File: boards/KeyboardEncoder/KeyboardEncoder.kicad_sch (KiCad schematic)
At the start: 30 parts, among them J1 ISP, J2 Encoder, J3 MIDI Out, J4 SelectRX, J5 MIDI In, J7 BoardCon, J8 PistonEncoder, U1 ATmega48-20P, U2 6N137, U3 74LS14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

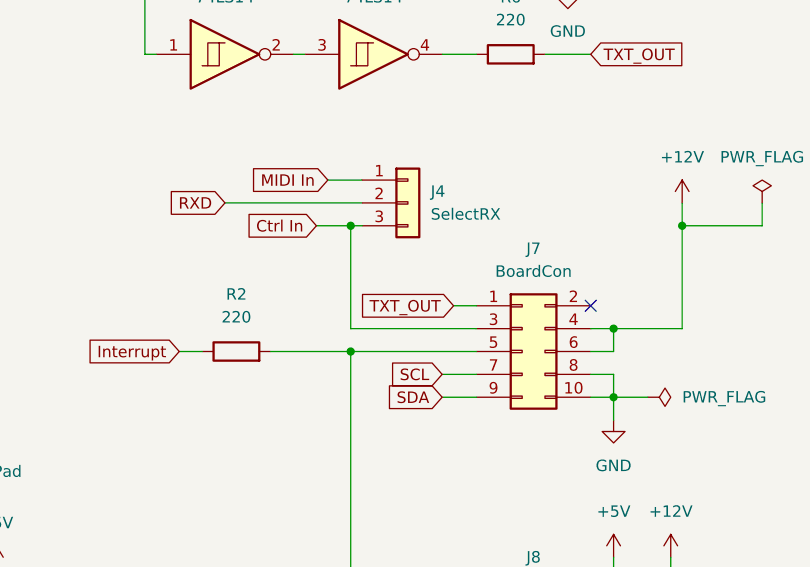
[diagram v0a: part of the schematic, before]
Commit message: Finished IO-Board PCB, switched RX/TX of board connectors for better routing
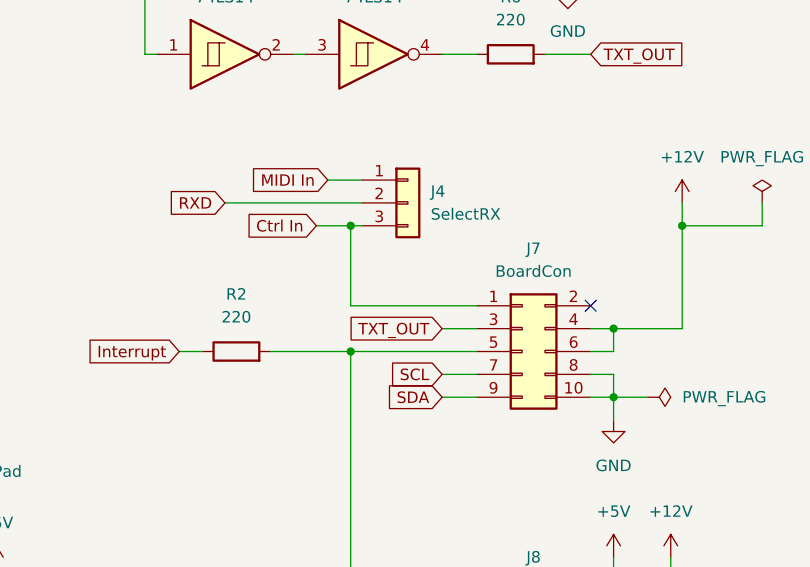
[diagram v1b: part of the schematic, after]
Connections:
- net Ctrl In: now also J7.1 (Pin_1); no longer J7.3 (Pin_3)
- net TXT_OUT: now also J7.3 (Pin_3); no longer J7.1 (Pin_1)

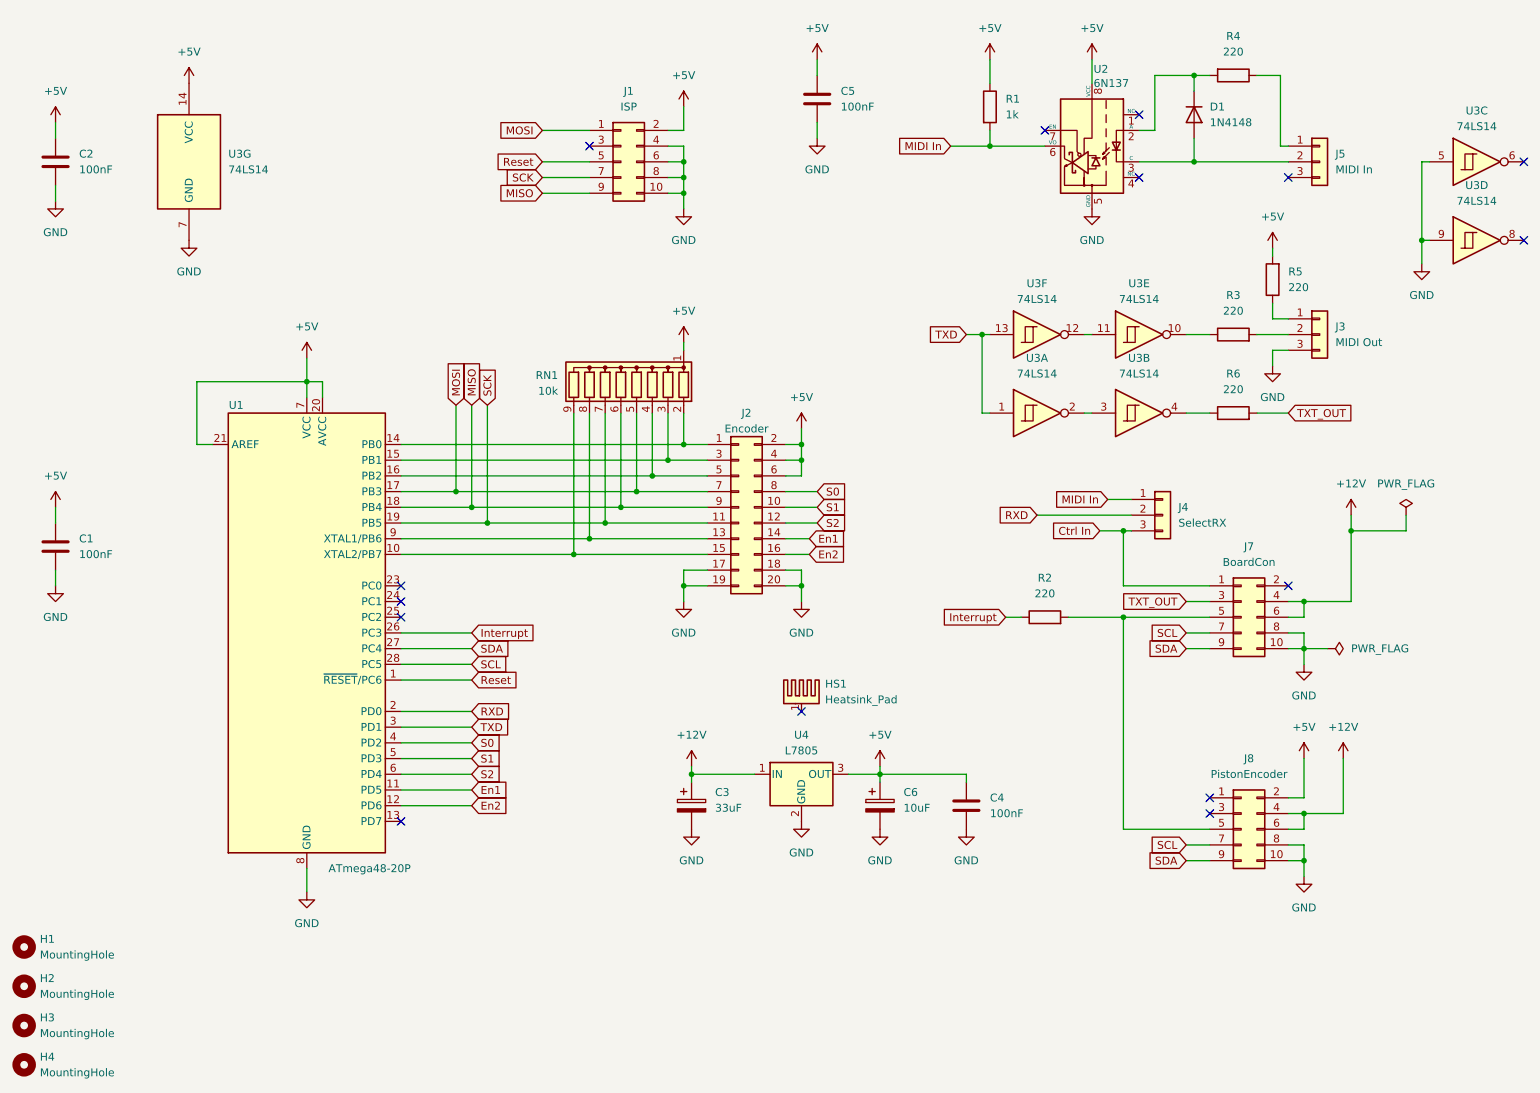
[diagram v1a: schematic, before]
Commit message: Fixed interrupt line to use open collector, added pullups to I2C lines
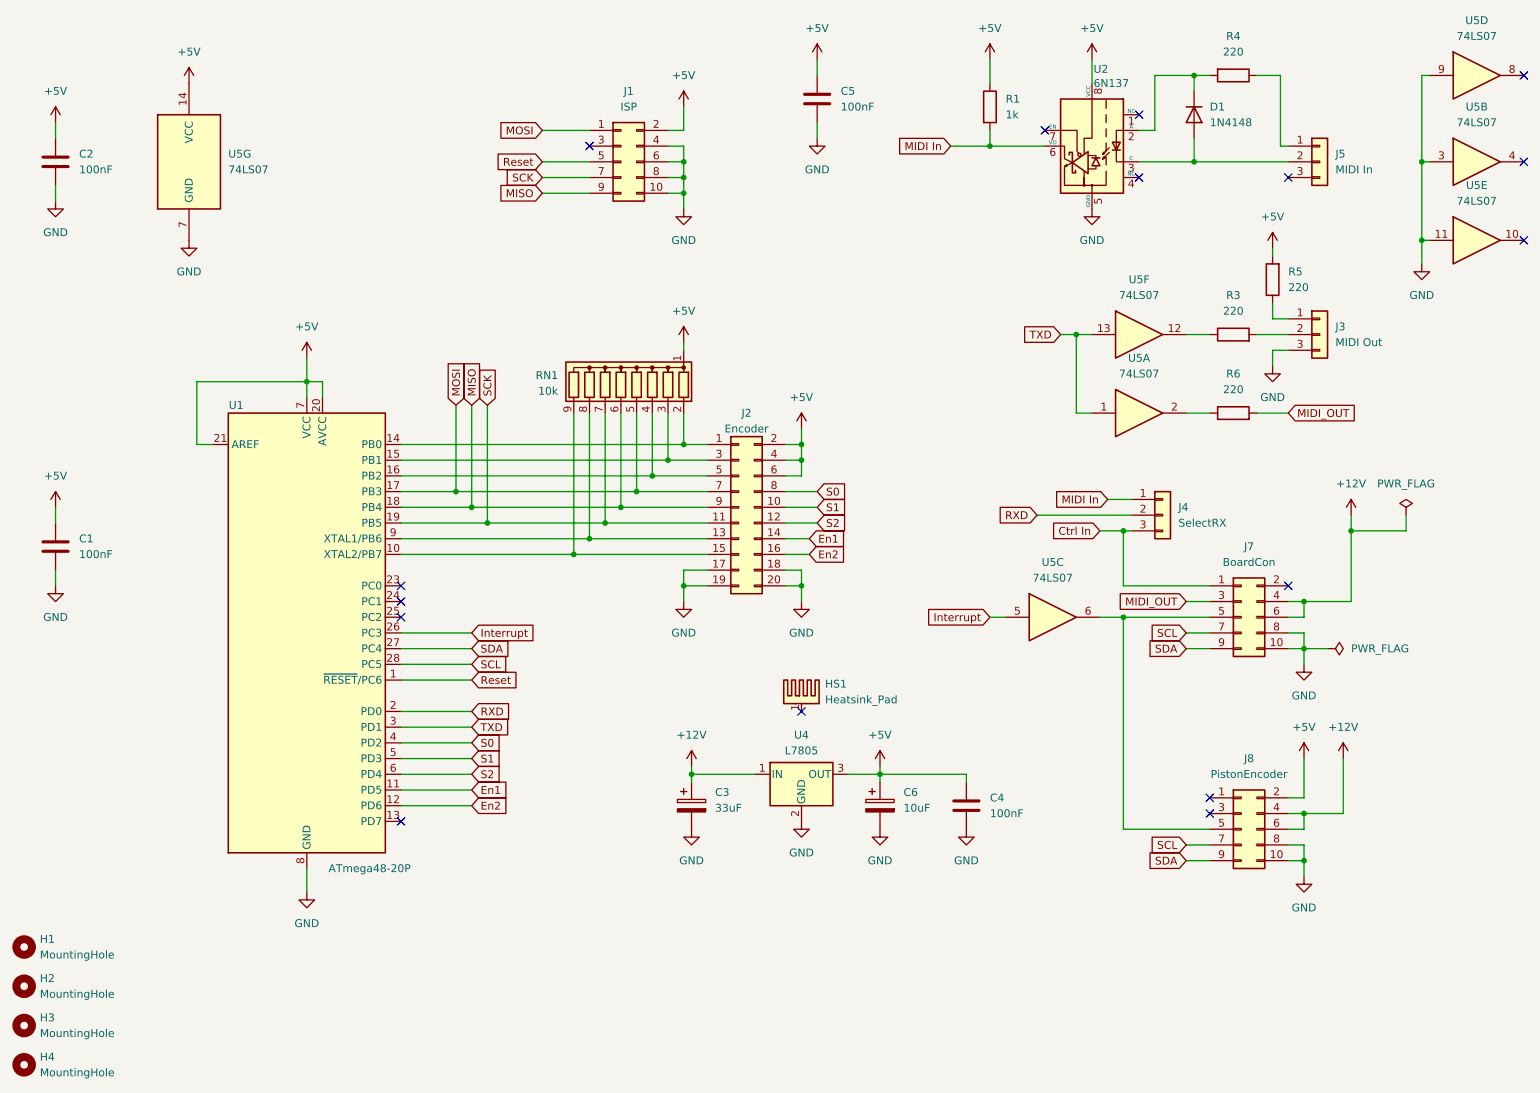
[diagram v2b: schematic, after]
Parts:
- removed R2: 220, Resistor_THT:R_Axial_DIN0204_L3.6mm_D1.6mm_P7.62mm_Horizontal, symbol Device:R
- removed U3: 74LS14, Package_DIP:DIP-14_W7.62mm, symbol 74xx:74LS14
- added U5: 74LS07, Package_DIP:DIP-14_W7.62mm, symbol 74xx:74LS07
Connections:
- net +5V: now also U5.14 (VCC)
- net GND: now also U5.11, U5.3, U5.7 (GND), U5.9
- net Interrupt: now also U5.5
- net TXD: now also U5.1, U5.13
- net at R6.1: now also U5.2
- net at R3.1: now also U5.12
- net at J7.5 (Pin_5), J8.5 (Pin_5): now also U5.6
- net TXT_OUT renamed MIDI_OUT
- no-connect marks 15 -> 16

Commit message: Added bypass caps to power supplies, use cheaper MAX232 IC.
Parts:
- added C7: 330nF, Capacitor_THT:C_Disc_D4.3mm_W1.9mm_P5.00mm, symbol Device:C
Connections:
- net +12V: now also C7.1
- net GND: now also C7.2
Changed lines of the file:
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@@
 	(wire
 		(pts
+			(xy 120.65 137.16) (xy 135.89 137.16)
+		)
+		(stroke
+			(width 0)
+			(type default)
+		)
+	)
+	(wire
+		(pts
 			(xy 232.41 151.13) (xy 234.95 151.13)
 		)
@@
 	(wire
 		(pts
+			(xy 120.65 138.43) (xy 120.65 137.16)
+		)
+		(stroke
+			(width 0)
+			(type default)
+		)
+	)
+	(wire
+		(pts
 			(xy 88.9 129.54) (xy 100.33 129.54)
 		)
@@
 	)
 	(symbol
+		(lib_id "Device:C")
+		(at 120.65 142.24 0)
+		(unit 1)
+		(exclude_from_sim no)
+		(in_bom yes)
+		(on_board yes)
+		(dnp no)
+		(fields_autoplaced yes)
+		(property "Reference" "C7"
+			(at 124.46 140.9699 0)
+			(effects
+				(font
+					(size 1.27 1.27)
+				)
+				(justify left)
+			)
+		)
+		(property "Value" "330nF"
+			(at 124.46 143.5099 0)
+			(effects
+				(font
+					(size 1.27 1.27)
+				)
+				(justify left)
+			)
+		)
+		(property "Footprint" "Capacitor_THT:C_Disc_D4.3mm_W1.9mm_P5.00mm"
+			(at 121.6152 146.05 0)
+			(effects
+				(font
+					(size 1.27 1.27)
+				)
+				(hide yes)
+			)
+		)
+		(property "Datasheet" "~"
+			(at 120.65 142.24 0)
+			(effects
+				(font
+					(size 1.27 1.27)
+				)
+				(hide yes)
+			)
+		)
+		(property "Description" "Unpolarized capacitor"
+			(at 120.65 142.24 0)
+			(effects
+				(font
+					(size 1.27 1.27)
+				)
+				(hide yes)
+			)
+		)
+		(pin "1"
+		)
+		(pin "2"
+		)
+		(instances
+			(project "KeyboardEncoder"
+				(path "/203cfae3-c134-4f8b-b17f-2675fc7b8ec3"
+					(reference "C7")
+					(unit 1)
+				)
+			)
+		)
+	)
+	(symbol
 		(lib_id "MCU_Microchip_ATmega:ATmega48-20P")
 		(at 73.66 114.3 0)
@@
 					(unit 1)
 				)
+			)
+		)
+	)
+	(symbol
+		(lib_id "power:GND")
+		(at 120.65 146.05 0)
+		(unit 1)
+		(exclude_from_sim no)
+		(in_bom yes)
+		(on_board yes)
+		(dnp no)
+		(fields_autoplaced yes)
+		(property "Reference" "#PWR017"
+			(at 120.65 152.4 0)
+			(effects
+				(font
+					(size 1.27 1.27)
+				)
+				(hide yes)
+			)
+		)
+		(property "Value" "GND"
+			(at 120.65 151.13 0)
+			(effects
+				(font
+					(size 1.27 1.27)
+				)
+			)
+		)
+		(property "Footprint" ""
+			(at 120.65 146.05 0)
+			(effects
+				(font
+					(size 1.27 1.27)
+				)
+				(hide yes)
+			)
+		)
+		(property "Datasheet" ""
+			(at 120.65 146.05 0)
+			(effects
+				(font
+					(size 1.27 1.27)
+				)
+				(hide yes)
+			)
+		)
+		(property "Description" "Power symbol creates a global label with name \"GND\" , ground"
+			(at 120.65 146.05 0)
+			(effects
+				(font
+					(size 1.27 1.27)
+				)
+				(hide yes)
+			)
+		)
+		(pin "1"
+		)
+		(instances
+			(project "KeyboardEncoder"
+				(path "/203cfae3-c134-4f8b-b17f-2675fc7b8ec3"
+					(reference "#PWR017")
+					(unit 1)
+				)

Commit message: Updated design rules to 0.32mm template and exported Gerber files
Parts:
- C6: footprint Capacitor_THT:CP_Radial_D6.3mm_P2.50mm -> Capacitor_THT:CP_Radial_D5.0mm_P2.00mm
- R1: footprint Resistor_THT:R_Axial_DIN0204_L3.6mm_D1.6mm_P2.54mm_Vertical -> Resistor_THT:R_Axial_DIN0207_L6.3mm_D2.5mm_P2.54mm_Vertical
- R3, R4, R5, R6: footprint Resistor_THT:R_Axial_DIN0204_L3.6mm_D1.6mm_P7.62mm_Horizontal -> Resistor_THT:R_Axial_DIN0207_L6.3mm_D2.5mm_P10.16mm_Horizontal
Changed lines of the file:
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@@
 			)
 		)
-		(property "Footprint" "Resistor_THT:R_Axial_DIN0204_L3.6mm_D1.6mm_P7.62mm_Horizontal"
+		(property "Footprint" "Resistor_THT:R_Axial_DIN0207_L6.3mm_D2.5mm_P10.16mm_Horizontal"
 			(at 223.52 80.518 90)
 			(effects
@@
 			)
 		)
-		(property "Footprint" "Resistor_THT:R_Axial_DIN0204_L3.6mm_D1.6mm_P2.54mm_Vertical"
+		(property "Footprint" "Resistor_THT:R_Axial_DIN0207_L6.3mm_D2.5mm_P2.54mm_Vertical"
 			(at 182.372 29.21 90)
 			(effects
@@
 			)
 		)
-		(property "Footprint" "Resistor_THT:R_Axial_DIN0204_L3.6mm_D1.6mm_P7.62mm_Horizontal"
+		(property "Footprint" "Resistor_THT:R_Axial_DIN0207_L6.3mm_D2.5mm_P10.16mm_Horizontal"
 			(at 223.52 22.352 90)
 			(effects
@@
 			)
 		)
-		(property "Footprint" "Resistor_THT:R_Axial_DIN0204_L3.6mm_D1.6mm_P7.62mm_Horizontal"
+		(property "Footprint" "Resistor_THT:R_Axial_DIN0207_L6.3mm_D2.5mm_P10.16mm_Horizontal"
 			(at 231.648 57.15 90)
 			(effects
@@
 			)
 		)
-		(property "Footprint" "Resistor_THT:R_Axial_DIN0204_L3.6mm_D1.6mm_P7.62mm_Horizontal"
+		(property "Footprint" "Resistor_THT:R_Axial_DIN0207_L6.3mm_D2.5mm_P10.16mm_Horizontal"
 			(at 223.52 67.818 90)
 			(effects
@@
 			)
 		)
-		(property "Footprint" "Capacitor_THT:CP_Radial_D6.3mm_P2.50mm"
+		(property "Footprint" "Capacitor_THT:CP_Radial_D5.0mm_P2.00mm"
 			(at 167.3352 146.05 0)
 			(effects
